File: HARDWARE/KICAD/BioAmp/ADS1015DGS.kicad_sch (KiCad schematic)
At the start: 12 parts, among them U1 ADS1015IDGS

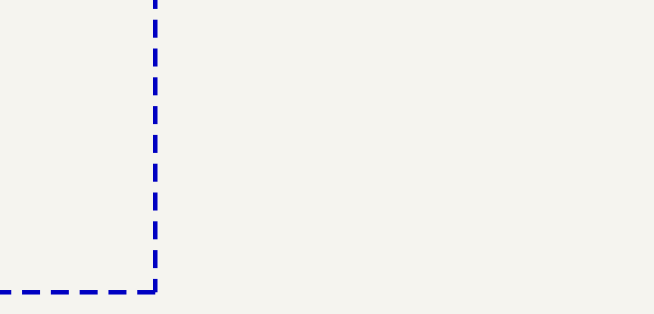
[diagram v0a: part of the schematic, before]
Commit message: Corrigido circuito AFE (Analog Front End); adição dos ports necessários na folha principal; transferência do LED de indicação de energia para folha de fontes; adição da sugestão para novo ADC.
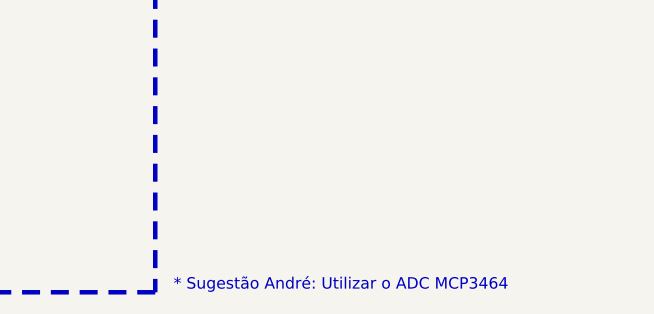
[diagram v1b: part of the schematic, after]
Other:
- note added: "* Sugestão André: Utilizar o ADC MCP3464"
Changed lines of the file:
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@@
+    (effects (font (size 1.27 1.27)) (justify left bottom))
+  )
+  (text "* Sugestão André: Utilizar o ADC MCP3464" (at 187.96 142.24 0)
     (effects (font (size 1.27 1.27)) (justify left bottom))
   )
